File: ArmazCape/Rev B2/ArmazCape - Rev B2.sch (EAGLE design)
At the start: 166 parts, among them J2 85505-5113, Q1 32.768kHz, 12.5pF, Q2 ASE, Q4 IRLML6344TRPBF, Q5 IRLML6344TRPBF, U1 L7985A, U13 L7985A, U19 DS1307ZN+, U20 24AA256-I/SN, U5 CD4050BD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

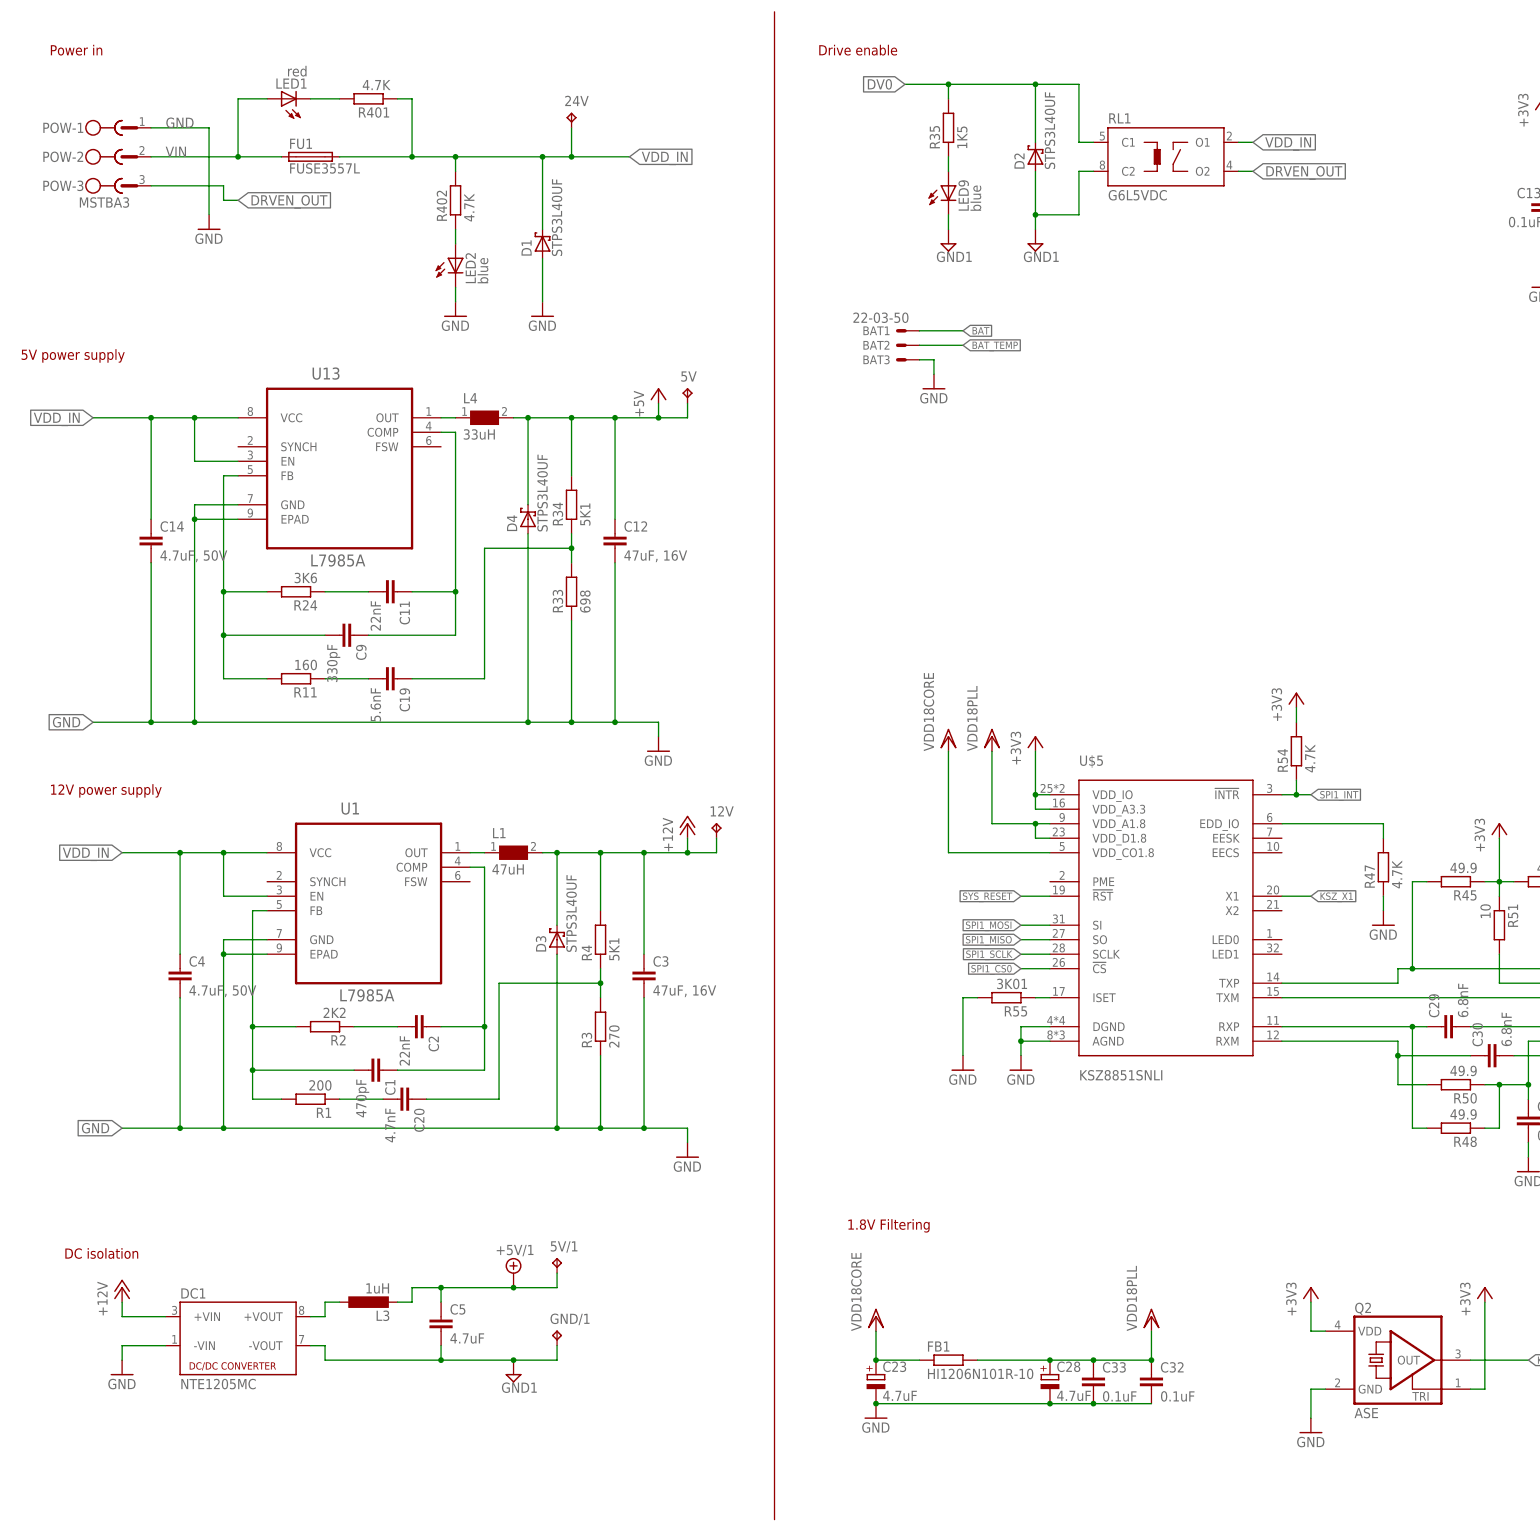
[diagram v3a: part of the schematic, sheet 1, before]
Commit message: Updated routed board - ArmazCape - Rev B2 This version doesn't provide isolated +5v; must be supplied via ArmazConnect
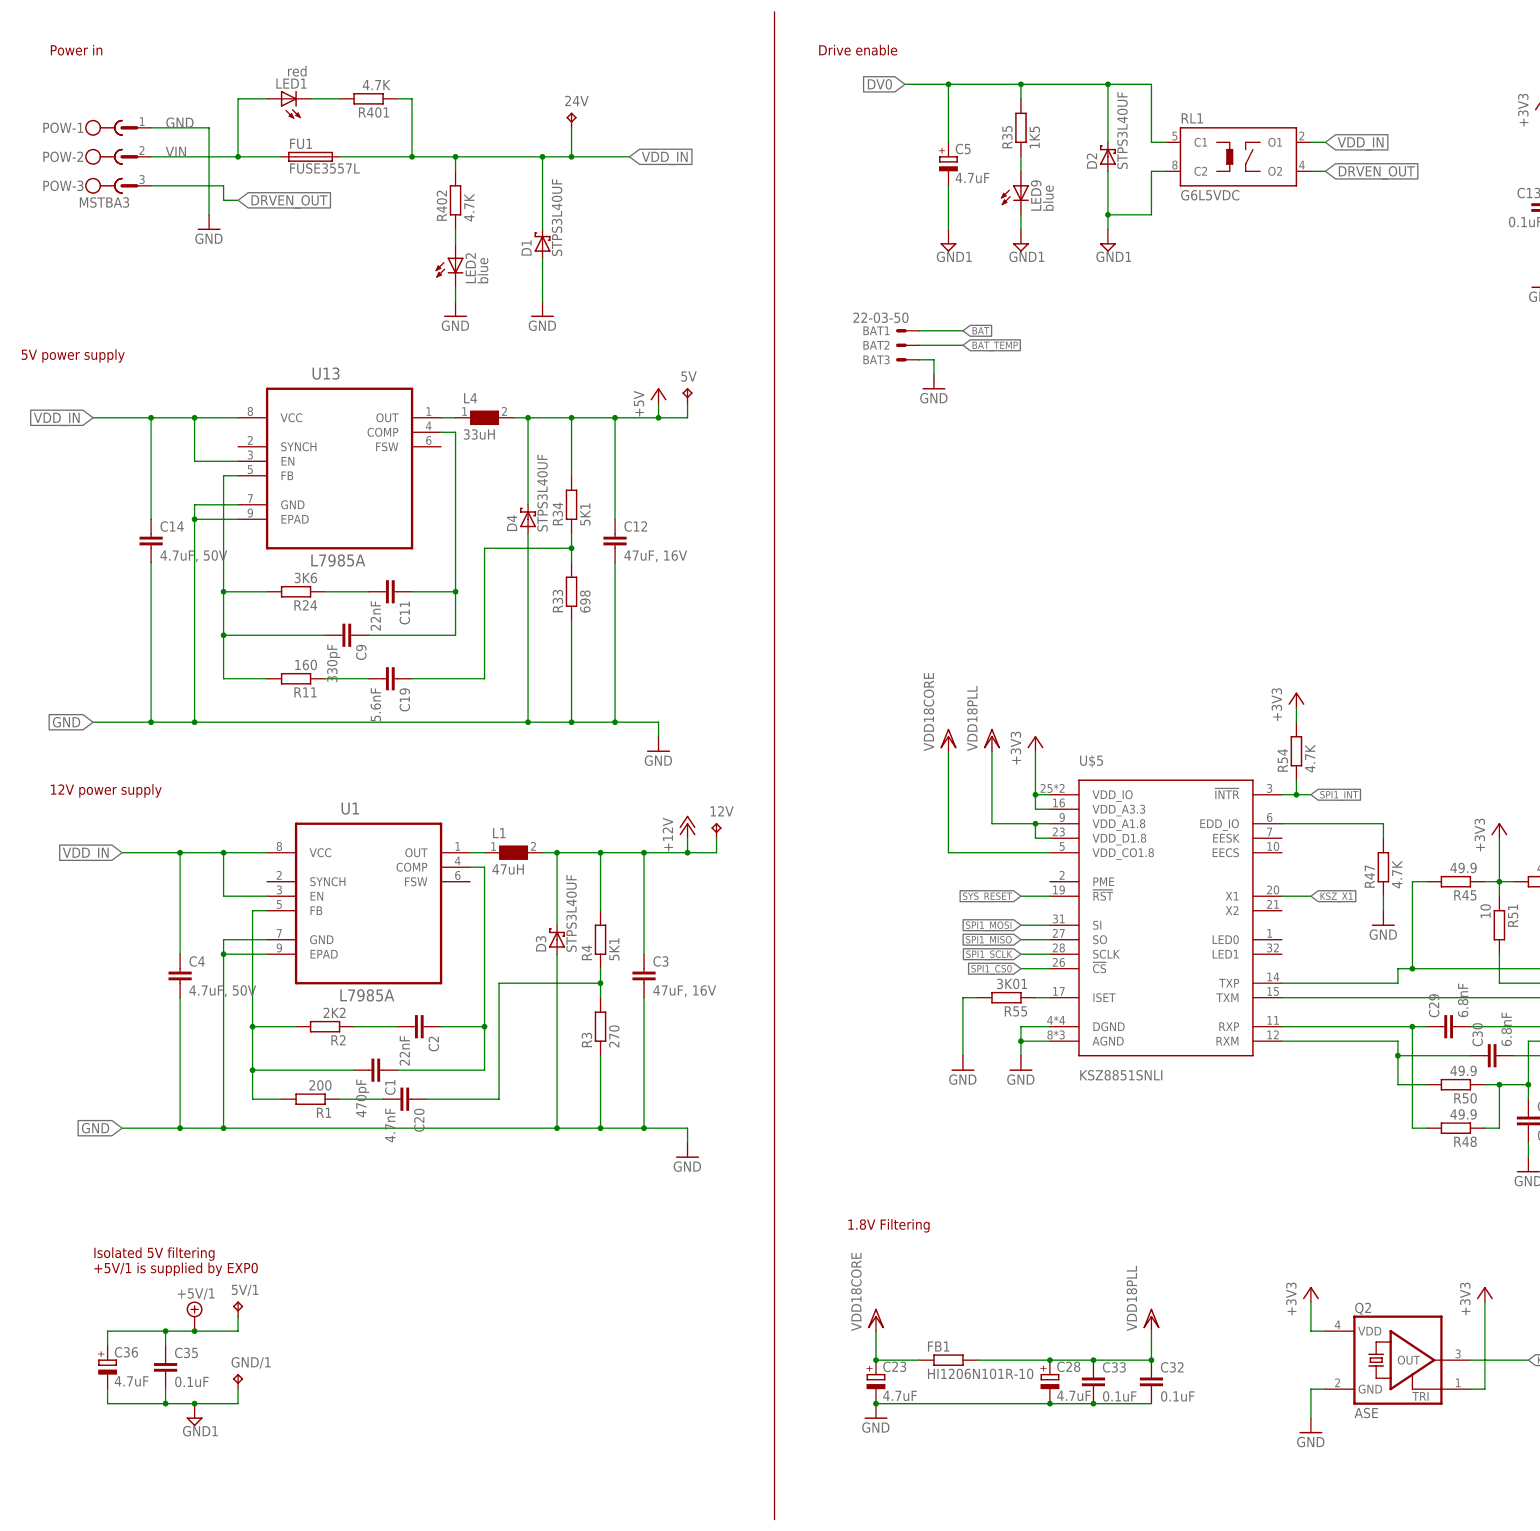
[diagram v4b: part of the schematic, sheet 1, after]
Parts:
- removed DC1: NTE1205MC, dc-dc-converter:NTE1205MC
- removed L3: 1uH, resistor-epcos:B82462G4102M000
- added C35: 0.1uF, rcl:C-EUC0603
- added C36: 4.7uF, rcl:CPOL-EUCT3216
- C5: device rcl:C-EUC0805 -> rcl:CPOL-EUCT3216; MF MULTICOMP -> AVX (FORMERLY KNOWN AS NICHICON); MPN MC0805X475K6R3CT -> F931A475MAA; OC_FARNELL 1759414 -> 1818579
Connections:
- removed net N$21: DC1.+VOUT, L3.1
- net +12V: no longer DC1.+VIN
- net +5V/1: now also C35.1, C36.+; no longer C5.1, L3.2
- net DV0: now also C5.+
- net GND: no longer DC1.-VIN
- net GND1: now also C35.2, C36.-, C5.-; no longer C5.2, DC1.-VOUT
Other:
- note added: "Isolated 5V filtering +5V/1 is supplied by EXP0"
- note removed: "DC isolation"
- moved on the sheet: 5V/1, D2, GND/1, LED9, R35, RL1

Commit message: Updated ArmazCape - Rev B2: Silkscreen for production Fixed bad Rev number on board.
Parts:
- removed U$5: KSZ8851SNLI, Micrel_By_element14_Batch_1:KSZ8851SNLI
- added U8: SN65HVD08D, ti:SN65HVD08D
- U9: value SN65HVD08D -> KSZ8851SNLI; device ti:SN65HVD08D -> Micrel_By_element14_Batch_1:KSZ8851SNLI; MF TEXAS INSTRUMENTS -> MICREL SEMICONDUCTOR; MPN (none) -> KSZ8851SNLI TR; OC_FARNELL (none) -> 1961911
- renumbered J2 to ETH0, U$4 to M1, U13 to U2, U19 to U3, U20 to U4
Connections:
- net +3V3: now also U9.VDD_IO; no longer U$5.VDD_IO
- net +5V/1: now also U8.VCC; no longer U9.VCC
- net DMX0-A: now also U8.A; no longer U9.A
- net DMX0-B: now also U8.B; no longer U9.B
- net GND: now also U9.AGND, U9.DGND; no longer U$5.AGND, U$5.DGND
- net GND1: now also U8.!RE, U8.DE, U8.GND; no longer U9.!RE, U9.DE, U9.GND
- net KSZ_X1: now also U9.X1; no longer U$5.X1
- net N$2000: now also U9.RXP; no longer U$5.RXP
- net N$27: now also U8.R; no longer U9.R
- net N$300: now also U9.RXM; no longer U$5.RXM
- net N$38: now also U9.ISET; no longer U$5.ISET
- net N$4200: now also U9.TXP; no longer U$5.TXP
- net N$4400: now also U9.TXM; no longer U$5.TXM
- net N$52: now also U9.EDD_IO; no longer U$5.EDD_IO
- net SPI1_CS0: now also U9.!CS; no longer U$5.!CS
- net SPI1_INT: now also U9.!INTR; no longer U$5.!INTR
- net SPI1_MISO: now also U9.SO; no longer U$5.SO
- net SPI1_MOSI: now also U9.SI; no longer U$5.SI
- net SPI1_SCLK: now also U9.SCLK; no longer U$5.SCLK
- net SYS_RESET: now also U9.!RST; no longer U$5.!RST
- net VDD18CORE: now also U9.VDD_CO1.8; no longer U$5.VDD_CO1.8
- net VDD18PLL: now also U9.VDD_A1.8, U9.VDD_D1.8; no longer U$5.VDD_A1.8, U$5.VDD_D1.8

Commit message: Added GERBER files for ArmazCape Rev B3
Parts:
- ISW: OC_FARNELL 9731660 -> (none)
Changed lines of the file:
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@@
 <attribute name="MF" value="MOLEX"/>
 <attribute name="MPN" value="22-05-7108"/>
-<attribute name="OC_FARNELL" value="9731660"/>
 </part>
 <part name="GND15" library="supply1" deviceset="GND" device=""/>
